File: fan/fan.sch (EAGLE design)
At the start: 3 parts

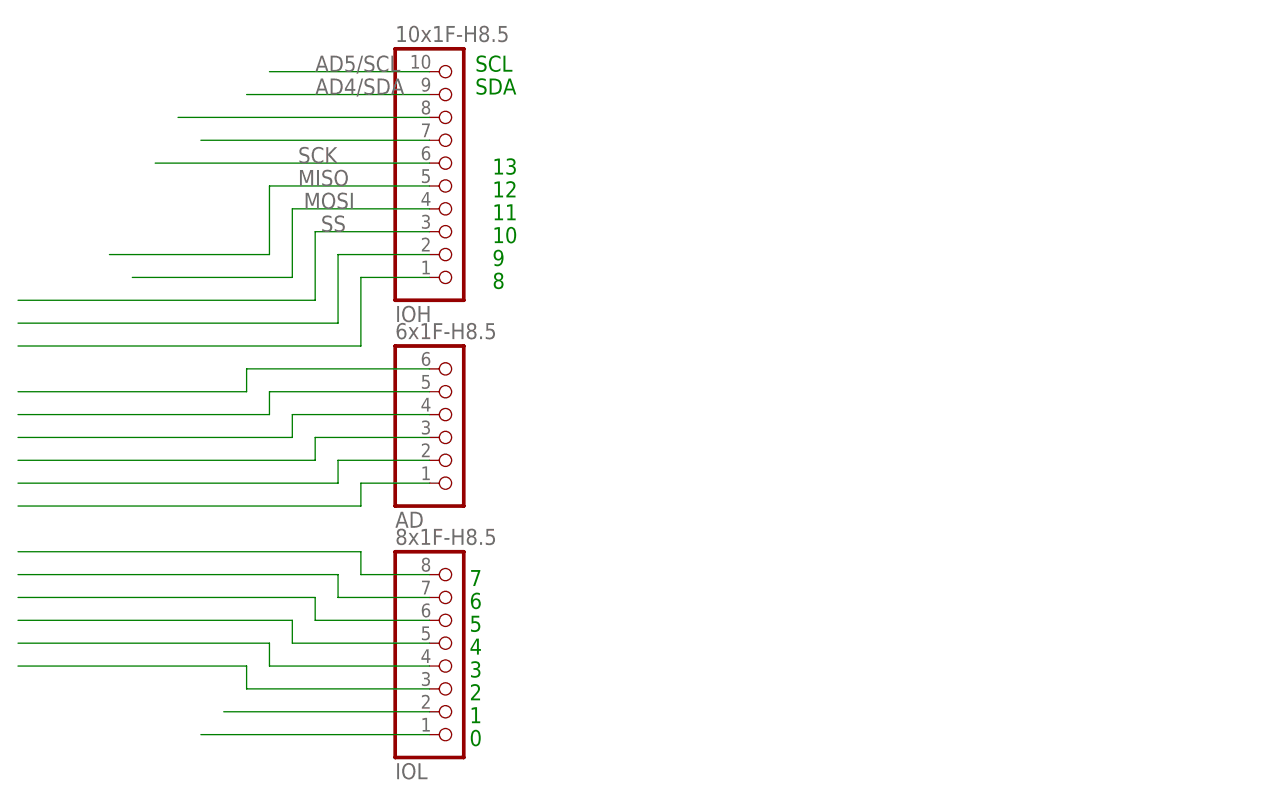
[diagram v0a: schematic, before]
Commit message: complete fan.sch
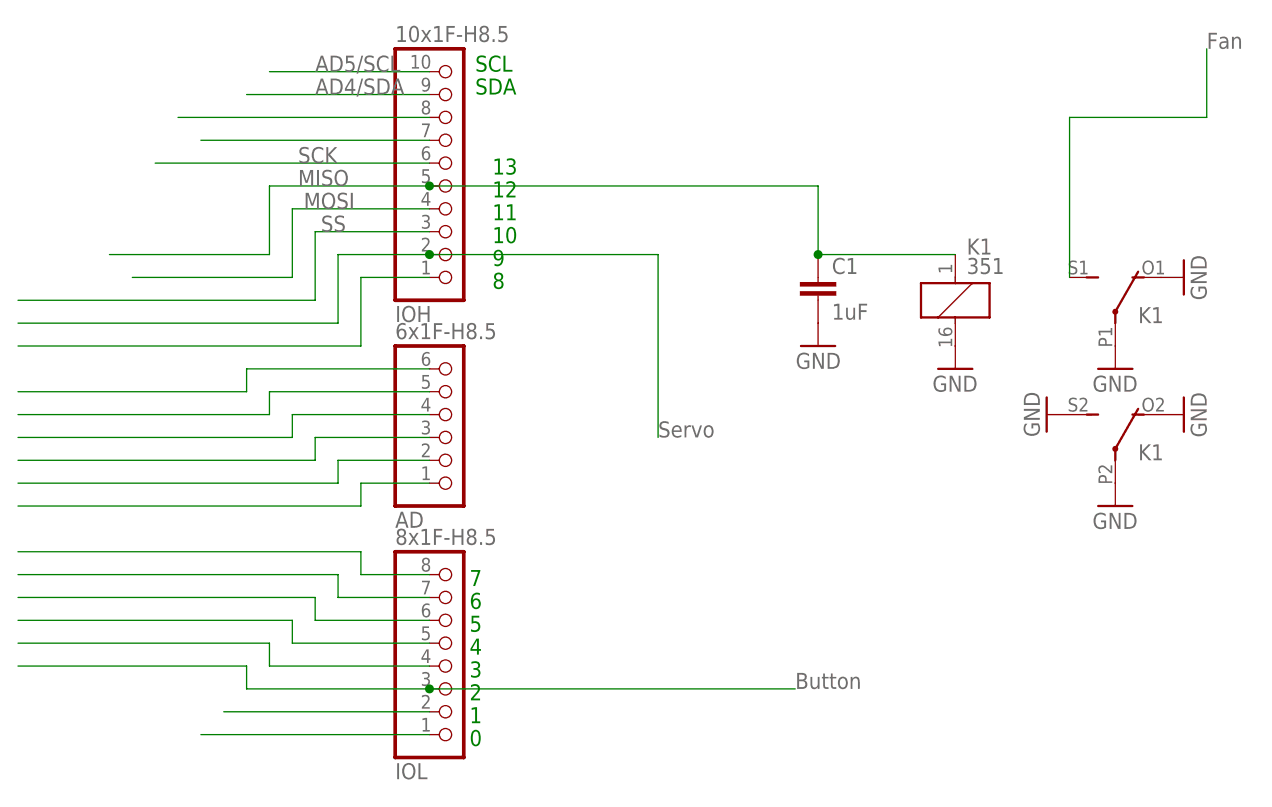
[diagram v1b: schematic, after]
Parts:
- added C1: 1uF, capacitor-wima:C2,5-3
- added K1: 351, relay:351
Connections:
- new net N$1: K12.S
- net GND: now also C1.2, K11.2, K12.O, K12.P, K13.O, K13.P, K13.S
- net MISO: now also C1.1, K11.1
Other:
- note added: "Button"
- note added: "Fan"
- note added: "Servo"
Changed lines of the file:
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@@
 <part name="IOH" library="SmartPrj" deviceset="PINHD-1X10_ARD" device="" value="10x1F-H8.5"/>
 <part name="AD" library="SmartPrj" deviceset="PINHD-1X6" device="" value="6x1F-H8.5"/>
+<part name="C1" library="capacitor-wima" deviceset="C" device="2,5-3" value="1uF"/>
+<part name="GND1" library="supply1" deviceset="GND" device=""/>
+<part name="K1" library="relay" deviceset="351" device=""/>
+<part name="GND2" library="supply1" deviceset="GND" device=""/>
+<part name="GND3" library="supply1" deviceset="GND" device=""/>
+<part name="GND4" library="supply1" deviceset="GND" device=""/>
+<part name="GND5" library="supply1" deviceset="GND" device=""/>
+<part name="GND6" library="supply1" deviceset="GND" device=""/>
+<part name="GND7" library="supply1" deviceset="GND" device=""/>
 </parts>
 <sheets>
@@
 <text x="68.58" y="83.82" size="1.778" layer="91">SDA</text>
 <text x="68.58" y="86.36" size="1.778" layer="91">SCL</text>
+<text x="149.86" y="88.9" size="1.778" layer="95">Fan</text>
+<text x="88.9" y="45.72" size="1.778" layer="95">Servo</text>
+<text x="104.14" y="17.78" size="1.778" layer="95">Button</text>
 </plain>
 <instances>
@@
 <instance part="IOH" gate="A" x="66.04" y="73.66" rot="MR180"/>
 <instance part="AD" gate="A" x="66.04" y="48.26" rot="MR180"/>
+<instance part="C1" gate="G$1" x="106.68" y="63.5"/>
+<instance part="GND1" gate="1" x="106.68" y="55.88" rot="MR0"/>
+<instance part="K1" gate="1" x="121.92" y="60.96"/>
+<instance part="K1" gate="2" x="139.7" y="58.42"/>
+<instance part="K1" gate="3" x="139.7" y="43.18"/>
+<instance part="GND2" gate="1" x="121.92" y="53.34"/>
+<instance part="GND3" gate="1" x="139.7" y="53.34"/>
+<instance part="GND4" gate="1" x="139.7" y="38.1"/>
+<instance part="GND5" gate="1" x="147.32" y="48.26" rot="R90"/>
+<instance part="GND6" gate="1" x="147.32" y="63.5" rot="R90"/>
+<instance part="GND7" gate="1" x="132.08" y="48.26" rot="R270"/>
 </instances>
 <busses>
@@
 <pinref part="IOH" gate="A" pin="7"/>
 </segment>
+<segment>
+<pinref part="C1" gate="G$1" pin="2"/>
+<pinref part="GND1" gate="1" pin="GND"/>
+</segment>
+<segment>
+<pinref part="K1" gate="1" pin="2"/>
+<pinref part="GND2" gate="1" pin="GND"/>
+</segment>
+<segment>
+<pinref part="K1" gate="2" pin="P"/>
+<pinref part="GND3" gate="1" pin="GND"/>
+</segment>
+<segment>
+<pinref part="K1" gate="3" pin="P"/>
+<pinref part="GND4" gate="1" pin="GND"/>
+</segment>
+<segment>
+<pinref part="K1" gate="3" pin="O"/>
+<pinref part="GND5" gate="1" pin="GND"/>
+</segment>
+<segment>
+<pinref part="K1" gate="2" pin="O"/>
+<pinref part="GND6" gate="1" pin="GND"/>
+</segment>
+<segment>
+<pinref part="K1" gate="3" pin="S"/>
+<pinref part="GND7" gate="1" pin="GND"/>
+</segment>
 </net>
 <net name="AREF" class="4">
@@
 <label x="48.895" y="73.66" size="1.778" layer="95"/>
 <pinref part="IOH" gate="A" pin="5"/>
+<pinref part="C1" gate="G$1" pin="1"/>
+<wire x1="106.68" y1="66.04" x2="121.92" y2="66.04" width="0.1524" layer="91"/>
+<junction x="106.68" y="66.04"/>
+<pinref part="K1" gate="1" pin="1"/>
+<wire x1="63.5" y1="73.66" x2="106.68" y2="73.66" width="0.1524" layer="91"/>
+<wire x1="106.68" y1="73.66" x2="106.68" y2="66.04" width="0.1524" layer="91"/>
+<junction x="63.5" y="73.66"/>
 </segment>
 </net>
@@
 <wire x1="43.18" y1="20.32" x2="17.78" y2="20.32" width="0.1524" layer="91"/>
 <pinref part="IOL" gate="A" pin="3"/>
+<wire x1="63.5" y1="17.78" x2="104.14" y2="17.78" width="0.1524" layer="91"/>
+<junction x="63.5" y="17.78"/>
 </segment>
 </net>
@@
 <wire x1="53.34" y1="58.42" x2="17.78" y2="58.42" width="0.1524" layer="91"/>
 <pinref part="IOH" gate="A" pin="2"/>
-</segment>
-</net>
+<wire x1="63.5" y1="66.04" x2="88.9" y2="66.04" width="0.1524" layer="91"/>
+<wire x1="88.9" y1="66.04" x2="88.9" y2="45.72" width="0.1524" layer="91"/>
+<junction x="63.5" y="66.04"/>
+</segment>
+</net>
+<net name="N$1" class="0">
+<segment>
+<pinref part="K1" gate="2" pin="S"/>
+<wire x1="134.62" y1="63.5" x2="134.62" y2="81.28" width="0.1524" layer="91"/>
+<wire x1="134.62" y1="81.28" x2="149.86" y2="81.28" width="0.1524" layer="91"/>
+<wire x1="149.86" y1="81.28" x2="149.86" y2="88.9" width="0.1524" layer="91"/>
+</segment>
+</net>

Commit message: update fan.sch
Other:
- note added: "A0"
- note added: "CS"
- note added: "MOSI"
- note added: "RST"
- note added: "SCK"
- note removed: "Servo"
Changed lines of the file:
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@@
 <text x="68.58" y="86.36" size="1.778" layer="91">SCL</text>
 <text x="149.86" y="88.9" size="1.778" layer="95">Fan</text>
-<text x="88.9" y="45.72" size="1.778" layer="95">Servo</text>
 <text x="104.14" y="17.78" size="1.778" layer="95">Button</text>
+<text x="104.14" y="20.32" size="1.778" layer="91">MOSI</text>
+<text x="104.14" y="22.86" size="1.778" layer="91">SCK</text>
+<text x="104.14" y="25.4" size="1.778" layer="91">A0</text>
+<text x="104.14" y="27.94" size="1.778" layer="91">RST</text>
+<text x="104.14" y="30.48" size="1.778" layer="91">CS</text>
 </plain>
 <instances>
@@
 <wire x1="45.72" y1="20.32" x2="63.5" y2="20.32" width="0.1524" layer="91"/>
 <pinref part="IOL" gate="A" pin="4"/>
+<wire x1="63.5" y1="20.32" x2="104.14" y2="20.32" width="0.1524" layer="91"/>
+<junction x="63.5" y="20.32"/>
 </segment>
 </net>
@@
 <wire x1="48.26" y1="25.4" x2="17.78" y2="25.4" width="0.1524" layer="91"/>
 <pinref part="IOL" gate="A" pin="5"/>
+<wire x1="63.5" y1="22.86" x2="104.14" y2="22.86" width="0.1524" layer="91"/>
+<junction x="63.5" y="22.86"/>
 </segment>
 </net>
@@
 <wire x1="50.8" y1="25.4" x2="63.5" y2="25.4" width="0.1524" layer="91"/>
 <pinref part="IOL" gate="A" pin="6"/>
+<wire x1="63.5" y1="25.4" x2="104.14" y2="25.4" width="0.1524" layer="91"/>
+<junction x="63.5" y="25.4"/>
 </segment>
 </net>
@@
 <wire x1="53.34" y1="30.48" x2="17.78" y2="30.48" width="0.1524" layer="91"/>
 <pinref part="IOL" gate="A" pin="7"/>
+<wire x1="63.5" y1="27.94" x2="104.14" y2="27.94" width="0.1524" layer="91"/>
+<junction x="63.5" y="27.94"/>
 </segment>
 </net>
@@
 <wire x1="55.88" y1="30.48" x2="63.5" y2="30.48" width="0.1524" layer="91"/>
 <pinref part="IOL" gate="A" pin="8"/>
+<wire x1="63.5" y1="30.48" x2="104.14" y2="30.48" width="0.1524" layer="91"/>
+<junction x="63.5" y="30.48"/>
 </segment>
 </net>
@@
 <wire x1="53.34" y1="58.42" x2="17.78" y2="58.42" width="0.1524" layer="91"/>
 <pinref part="IOH" gate="A" pin="2"/>
-<wire x1="63.5" y1="66.04" x2="88.9" y2="66.04" width="0.1524" layer="91"/>
-<wire x1="88.9" y1="66.04" x2="88.9" y2="45.72" width="0.1524" layer="91"/>
-<junction x="63.5" y="66.04"/>
-</segment>
-</net>
+</segment>
+</net>
